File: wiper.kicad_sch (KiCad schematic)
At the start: 64 parts, among them J1 Conn_01x02, J10 Conn_01x02, J2 Sensor FW, J3 Sensor BK, J4 Conn_01x02, J5 Conn_01x02, J6 PROG, J7 I2C, J8 UART, J9 Conn_01x02, K1 G5LE-1, K2 G5LE-1, Q1 MMBT2222A, Q2 MMBT2222A, Q3 MMBT2222A, Q4 MMBT2222A, SW1 Reset, U1 LM7805_TO220, U2 PC817, U3 PC817, U4 KA78M05_TO252, U5 ATmega48-20A, Y1 16MHz

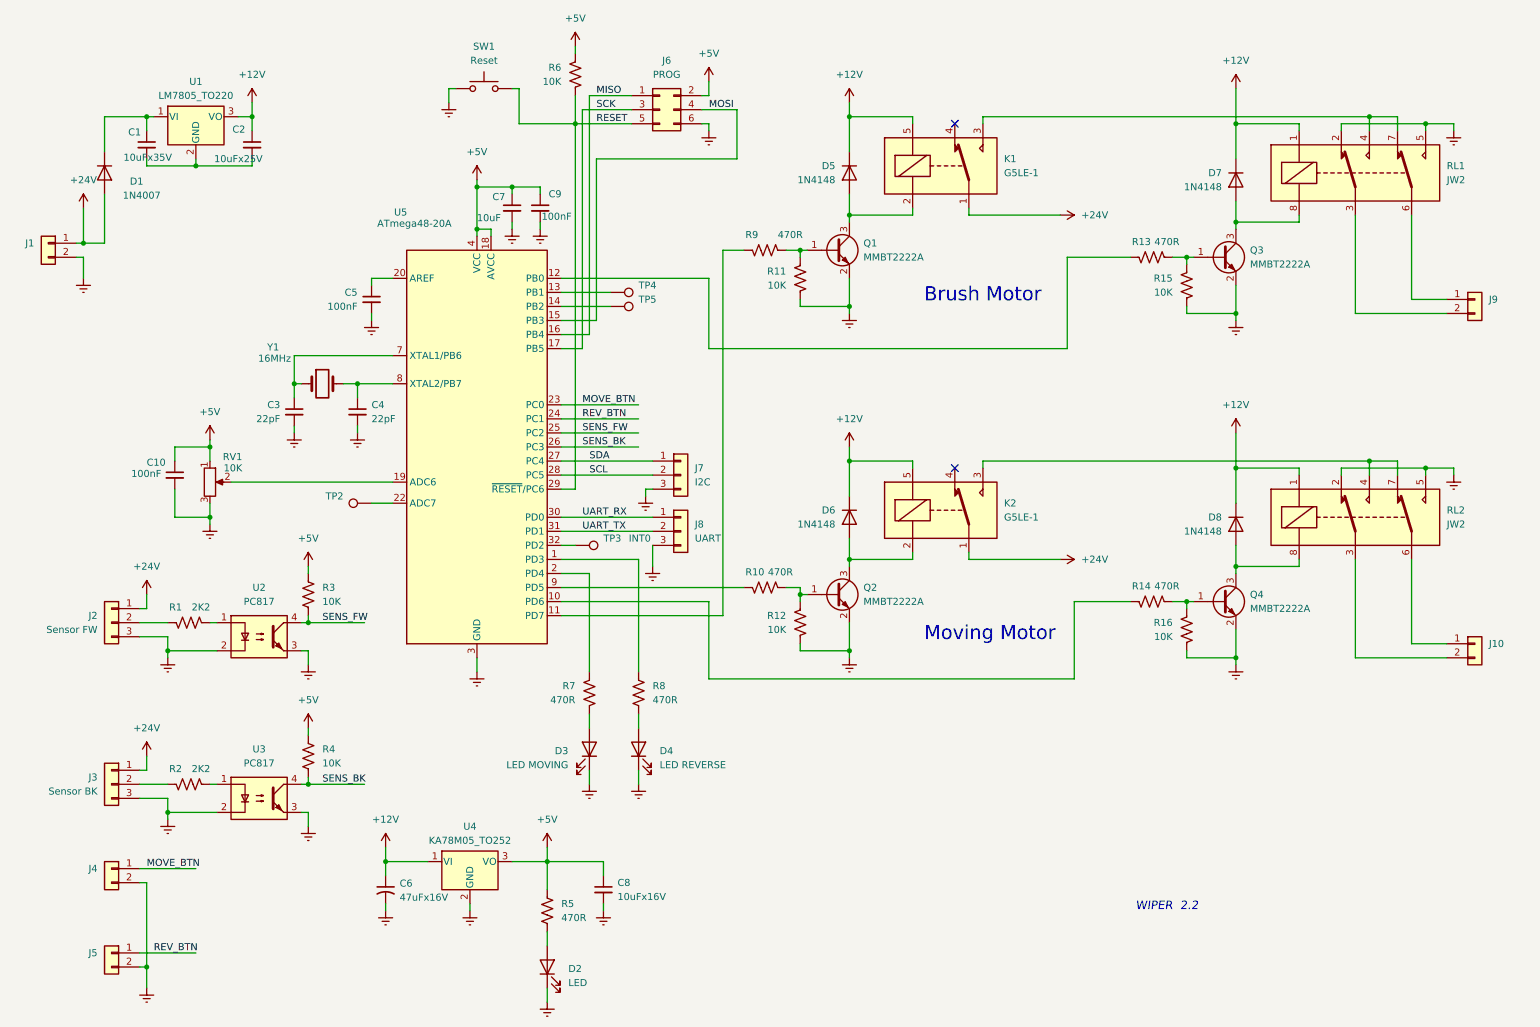
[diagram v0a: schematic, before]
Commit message: Schematic rework for v2
- Add RV2 (10K pot), Q5/Q6 (MMBT2222A), C11 (100nF), C12 (47uF/100V input cap)
- Remove LEDs D3/D4 and test point TP2
- Replace CUI terminal blocks with MetzConnect; J4/J5 changed to 3-pin (MOVE_BTN, REV_BTN)
- Change RV1 footprint to Piher PT-6
- Change D5-D8 to 1N4148W (SOD-123), C10/C11 to 0805
- Rearrange power supply section
- Add PWR_FLAG to input power nets (fixes ERC)
- Set U1 value to LM7812 (12V switching module, 78xx pinout)
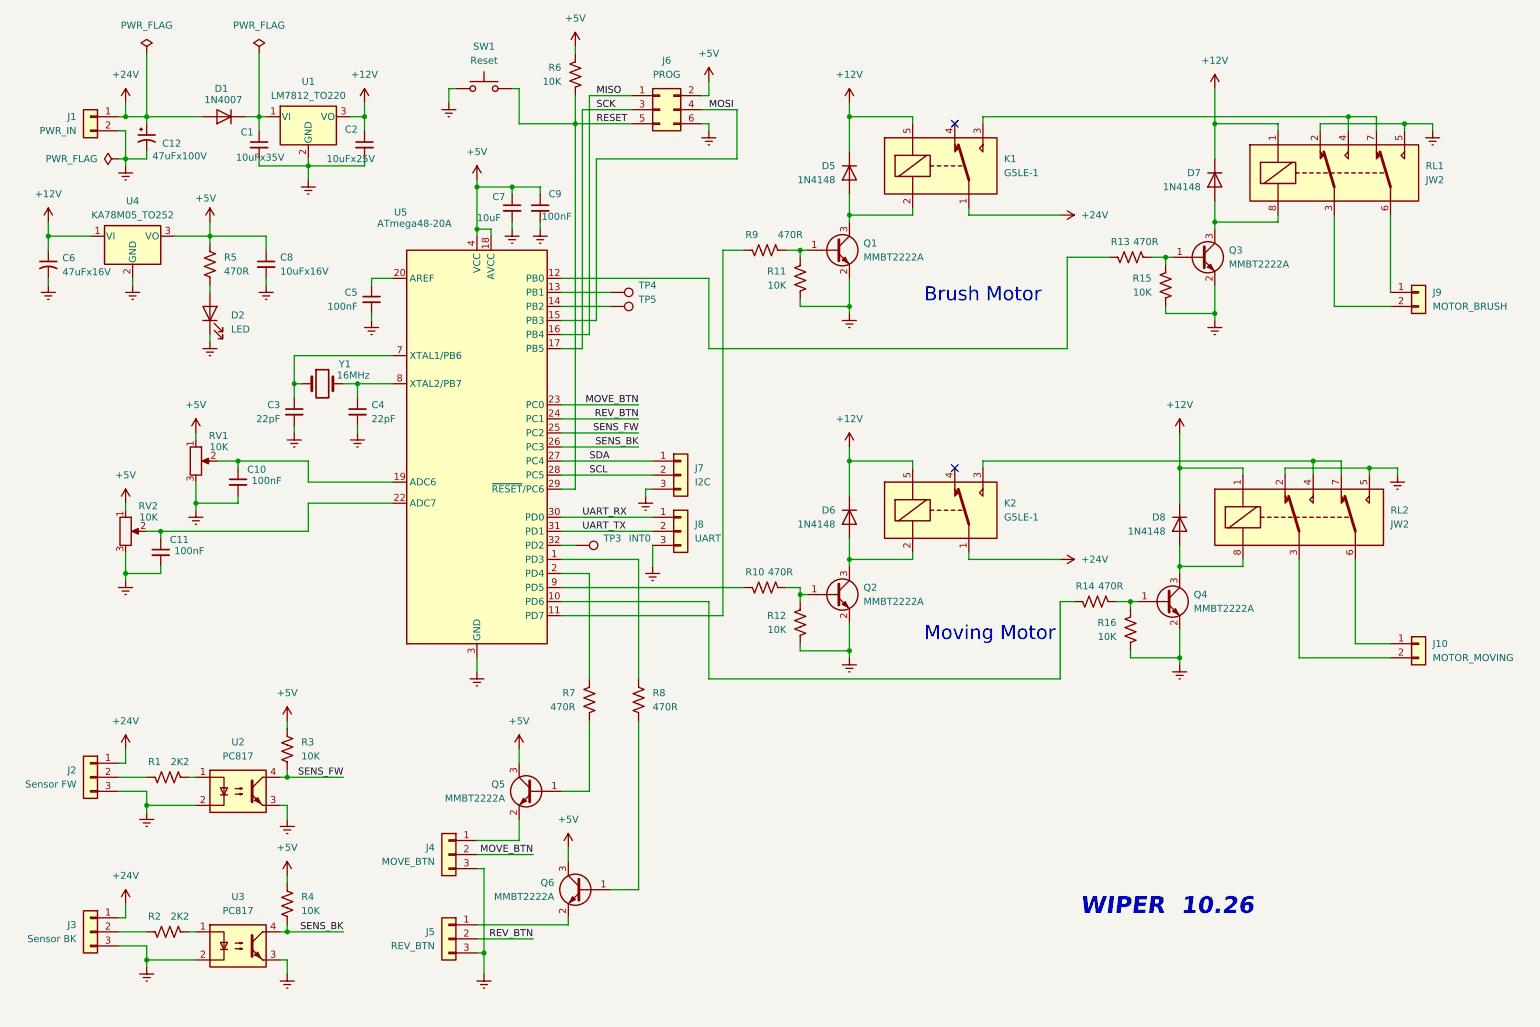
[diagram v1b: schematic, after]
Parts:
- removed D3: LED MOVING, LED_THT:LED_D3.0mm, symbol Device:LED
- removed D4: LED REVERSE, LED_THT:LED_D3.0mm, symbol Device:LED
- removed J4, J5: Conn_01x02, TerminalBlock_CUI:TerminalBlock_CUI_TB007-508-02_1x02_P5.08mm_Horizontal, symbol Connector_Generic:Conn_01x02
- removed TP2: ~, Connector_PinHeader_1.00mm:PinHeader_1x01_P1.00mm_Vertical, symbol Connector:TestPoint
- added C11: 100nF, Resistor_SMD:R_0805_2012Metric_Pad1.20x1.40mm_HandSolder, symbol Device:C_Small
- added C12: 47uFx100V, Capacitor_THT:C_Radial_D8.0mm_H7.0mm_P3.50mm, symbol Device:C_Polarized_Small_US
- added J4: MOVE_BTN, TerminalBlock_MetzConnect:TerminalBlock_MetzConnect_Type055_RT01503HDWU_1x03_P5.00mm_Horizontal, symbol Connector_Generic:Conn_01x03
- added J5: REV_BTN, TerminalBlock_MetzConnect:TerminalBlock_MetzConnect_Type055_RT01503HDWU_1x03_P5.00mm_Horizontal, symbol Connector_Generic:Conn_01x03
- added Q5, Q6: MMBT2222A, Package_TO_SOT_SMD:SOT-23, symbol Transistor_BJT:MMBT2222A
- added RV2: 10K, Potentiometer_THT:Potentiometer_Piher_PT-6-V_Vertical, symbol Device:R_Potentiometer
- C10: footprint Resistor_SMD:R_0603_1608Metric_Pad0.98x0.95mm_HandSolder -> Resistor_SMD:R_0805_2012Metric_Pad1.20x1.40mm_HandSolder
- D5, D6, D7, D8: footprint Diode_SMD:D_MiniMELF_Handsoldering -> Diode_SMD:D_SOD-123
- J1: value Conn_01x02 -> PWR_IN; footprint TerminalBlock_CUI:TerminalBlock_CUI_TB007-508-02_1x02_P5.08mm_Horizontal -> TerminalBlock_MetzConnect:TerminalBlock_MetzConnect_Type101_RT01602HBWC_1x02_P5.08mm_Horizontal
- J10: value Conn_01x02 -> MOTOR_MOVING; footprint TerminalBlock_CUI:TerminalBlock_CUI_TB007-508-02_1x02_P5.08mm_Horizontal -> TerminalBlock_MetzConnect:TerminalBlock_MetzConnect_Type101_RT01602HBWC_1x02_P5.08mm_Horizontal
- J2, J3: footprint TerminalBlock_CUI:TerminalBlock_CUI_TB007-508-03_1x03_P5.08mm_Horizontal -> TerminalBlock_MetzConnect:TerminalBlock_MetzConnect_Type055_RT01503HDWU_1x03_P5.00mm_Horizontal
- J9: value Conn_01x02 -> MOTOR_BRUSH; footprint TerminalBlock_CUI:TerminalBlock_CUI_TB007-508-02_1x02_P5.08mm_Horizontal -> TerminalBlock_MetzConnect:TerminalBlock_MetzConnect_Type101_RT01602HBWC_1x02_P5.08mm_Horizontal
- RV1: footprint Potentiometer_THT:Potentiometer_ACP_CA9-V10_Vertical -> Potentiometer_THT:Potentiometer_Piher_PT-6-V_Vertical
- U1: value LM7805_TO220 -> LM7812_TO220
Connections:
- net +24V: now also C12.1
- net +5V: now also Q5.3 (C), Q6.3 (C), RV2.1; no longer C10.1
- net MOVE_BTN: now also J4.2 (Pin_2)
- net REV_BTN: now also J5.2 (Pin_2)
- net at R7.2: now also Q5.1 (B)
- net at RV1.2, U5.19 (ADC6): now also C10.1
- net at U5.22 (ADC7): now also C11.1, RV2.2
- net at J1.2 (Pin_2): now also C12.2
- net at R8.2: now also Q6.1 (B)
- new net: J5.1 (Pin_1), Q6.2 (E)
- new net: J4.3 (Pin_3), J5.3 (Pin_3)
- new net: J4.1 (Pin_1), Q5.2 (E)
- new net: C11.2, RV2.3
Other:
- note added: "WIPER 10.26"
- note removed: "WIPER 2.2"
- moved on the sheet: C1, C10, C2, C6, C8, D1, D2, D7, D8, J1, J10, J2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

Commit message: Use hand-solder capacitor footprints, name J1/J9/J10, fix D5-D8 value (1N4148W)
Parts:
- C1, C2: footprint Resistor_SMD:R_1206_3216Metric -> Capacitor_SMD:C_1206_3216Metric
- C10, C11, C5, C7, C8: footprint Resistor_SMD:R_0805_2012Metric_Pad1.20x1.40mm_HandSolder -> Capacitor_SMD:C_0805_2012Metric_Pad1.18x1.45mm_HandSolder
- C3, C4, C9: footprint Resistor_SMD:R_0603_1608Metric_Pad0.98x0.95mm_HandSolder -> Capacitor_SMD:C_0603_1608Metric_Pad1.08x0.95mm_HandSolder
- D5, D6, D7, D8: value 1N4148 -> 1N4148W
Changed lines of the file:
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@@
 			)
 		)
-		(property "Value" "1N4148"
+		(property "Value" "1N4148W"
 			(at 162.56 105.4099 90)
 			(effects
@@
 			)
 		)
-		(property "Value" "1N4148"
+		(property "Value" "1N4148W"
 			(at 222.25 106.6799 90)
 			(effects
@@
 			)
 		)
-		(property "Value" "1N4148"
+		(property "Value" "1N4148W"
 			(at 228.6 44.4499 90)
 			(effects
@@
 			)
 		)
-		(property "Footprint" "Resistor_SMD:R_0603_1608Metric_Pad0.98x0.95mm_HandSolder"
+		(property "Footprint" "Capacitor_SMD:C_0603_1608Metric_Pad1.08x0.95mm_HandSolder"
 			(at 109.22 48.26 0)
 			(effects
@@
 			)
 		)
-		(property "Footprint" "Resistor_SMD:R_0805_2012Metric_Pad1.20x1.40mm_HandSolder"
+		(property "Footprint" "Capacitor_SMD:C_0805_2012Metric_Pad1.18x1.45mm_HandSolder"
 			(at 104.14 48.26 0)
 			(effects
@@
 			)
 		)
-		(property "Footprint" "Resistor_SMD:R_1206_3216Metric"
+		(property "Footprint" "Capacitor_SMD:C_1206_3216Metric"
 			(at 58.42 36.83 0)
 			(effects
@@
 			)
 		)
-		(property "Value" "1N4148"
+		(property "Value" "1N4148W"
 			(at 162.56 43.1799 90)
 			(effects
@@
 			)
 		)
-		(property "Footprint" "Resistor_SMD:R_1206_3216Metric"
+		(property "Footprint" "Capacitor_SMD:C_1206_3216Metric"
 			(at 77.47 36.83 0)
 			(effects
@@
 			)
 		)
-		(property "Footprint" "Resistor_SMD:R_0603_1608Metric_Pad0.98x0.95mm_HandSolder"
+		(property "Footprint" "Capacitor_SMD:C_0603_1608Metric_Pad1.08x0.95mm_HandSolder"
 			(at 64.77 85.09 0)
 			(effects
@@
 			)
 		)
-		(property "Footprint" "Resistor_SMD:R_0805_2012Metric_Pad1.20x1.40mm_HandSolder"
+		(property "Footprint" "Capacitor_SMD:C_0805_2012Metric_Pad1.18x1.45mm_HandSolder"
 			(at 40.64 110.49 0)
 			(effects
@@
 			)
 		)
-		(property "Footprint" "Resistor_SMD:R_0603_1608Metric_Pad0.98x0.95mm_HandSolder"
+		(property "Footprint" "Capacitor_SMD:C_0603_1608Metric_Pad1.08x0.95mm_HandSolder"
 			(at 76.2 85.09 0)
 			(effects
@@
 			)
 		)
-		(property "Footprint" "Resistor_SMD:R_0805_2012Metric_Pad1.20x1.40mm_HandSolder"
+		(property "Footprint" "Capacitor_SMD:C_0805_2012Metric_Pad1.18x1.45mm_HandSolder"
 			(at 54.61 97.79 0)
 			(effects
@@
 			)
 		)
-		(property "Footprint" "Resistor_SMD:R_0805_2012Metric_Pad1.20x1.40mm_HandSolder"
+		(property "Footprint" "Capacitor_SMD:C_0805_2012Metric_Pad1.18x1.45mm_HandSolder"
 			(at 78.74 64.77 0)
 			(effects
@@
 			)
 		)
-		(property "Footprint" "Resistor_SMD:R_0805_2012Metric_Pad1.20x1.40mm_HandSolder"
+		(property "Footprint" "Capacitor_SMD:C_0805_2012Metric_Pad1.18x1.45mm_HandSolder"
 			(at 59.69 58.42 0)
 			(effects

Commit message: New tracing finished. No mounting holes.
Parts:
- J4, J5: footprint TerminalBlock_MetzConnect:TerminalBlock_MetzConnect_Type055_RT01503HDWU_1x03_P5.00mm_Horizontal -> Connector_Molex:Molex_KK-254_AE-6410-03A_1x03_P2.54mm_Vertical
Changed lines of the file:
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@@
 			)
 		)
-		(property "Footprint" "TerminalBlock_MetzConnect:TerminalBlock_MetzConnect_Type055_RT01503HDWU_1x03_P5.00mm_Horizontal"
+		(property "Footprint" "Connector_Molex:Molex_KK-254_AE-6410-03A_1x03_P2.54mm_Vertical"
 			(at 92.71 180.34 0)
 			(effects
@@
 			)
 		)
-		(property "Footprint" "TerminalBlock_MetzConnect:TerminalBlock_MetzConnect_Type055_RT01503HDWU_1x03_P5.00mm_Horizontal"
+		(property "Footprint" "Connector_Molex:Molex_KK-254_AE-6410-03A_1x03_P2.54mm_Vertical"
 			(at 92.71 165.1 0)
 			(effects
